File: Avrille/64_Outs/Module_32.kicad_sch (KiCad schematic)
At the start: 9 parts, among them J8 DIN41612_02x32_AC, U6 74HC595, U7 74HC595, U8 74HC595, U9 74HC595

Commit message: reset
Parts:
- added F3: Fuse, Fuse:Fuseholder_Clip-5x20mm_Bel_FC-203-22_Lateral_P17.80x5.00mm_D1.17mm_Horizontal, symbol Device:Fuse
- added RN3, RN5, RN7, RN9: R_Pack08, Package_DIP:DIP-16_W7.62mm, symbol Device:R_Pack08
- C10: renamed from C7; footprint Capacitor_THT:C_Disc_D5.0mm_W2.5mm_P2.50mm -> Capacitor_THT:C_Disc_D4.3mm_W1.9mm_P5.00mm
- C11: renamed from C8; footprint Capacitor_THT:C_Disc_D5.0mm_W2.5mm_P2.50mm -> Capacitor_THT:C_Disc_D4.3mm_W1.9mm_P5.00mm
- C12: renamed from C9; footprint Capacitor_THT:C_Disc_D5.0mm_W2.5mm_P2.50mm -> Capacitor_THT:C_Disc_D4.3mm_W1.9mm_P5.00mm
- C13: renamed from C10; footprint Capacitor_THT:C_Disc_D5.0mm_W2.5mm_P2.50mm -> Capacitor_THT:C_Disc_D4.3mm_W1.9mm_P5.00mm
- U10: renamed from U6; footprint Package_SO:SOIC-16W_7.5x12.8mm_P1.27mm -> Package_DIP:CERDIP-16_W7.62mm_SideBrazed
- U11: renamed from U7; footprint Package_SO:SOIC-16W_7.5x12.8mm_P1.27mm -> Package_DIP:CERDIP-16_W7.62mm_SideBrazed
- U12: renamed from U8; footprint Package_SO:SOIC-16W_7.5x12.8mm_P1.27mm -> Package_DIP:CERDIP-16_W7.62mm_SideBrazed
- U13: renamed from U9; footprint Package_SO:SOIC-16W_7.5x12.8mm_P1.27mm -> Package_DIP:CERDIP-16_W7.62mm_SideBrazed
- renumbered J8 to J9
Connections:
- net GND: no longer J9.a17 (Pin_a17), J9.a18 (Pin_a18), J9.a19 (Pin_a19), J9.a20 (Pin_a20), J9.a21 (Pin_a21), J9.a22 (Pin_a22), J9.a23 (Pin_a23), J9.a24 (Pin_a24), J9.a25 (Pin_a25), J9.a26 (Pin_a26), J9.a27 (Pin_a27), J9.a28 (Pin_a28), J9.a29 (Pin_a29), J9.a30 (Pin_a30), J9.a31 (Pin_a31), J9.a32 (Pin_a32)
- net Sorties_10/IN_1: now also RN9.1 (R1.1); no longer U12.7 (QH)
- net Sorties_10/IN_2: now also RN9.2 (R2.1); no longer U12.6 (QG)
- net Sorties_10/IN_3: now also RN9.3 (R3.1); no longer U12.5 (QF)
- net Sorties_10/IN_4: now also RN9.4 (R4.1); no longer U12.4 (QE)
- net Sorties_10/V_IN: now also F3.1; no longer J9.a1 (Pin_a1), J9.a10 (Pin_a10), J9.a11 (Pin_a11), J9.a12 (Pin_a12), J9.a13 (Pin_a13), J9.a14 (Pin_a14), J9.a15 (Pin_a15), J9.a16 (Pin_a16), J9.a2 (Pin_a2), J9.a3 (Pin_a3), J9.a4 (Pin_a4), J9.a5 (Pin_a5), J9.a6 (Pin_a6), J9.a7 (Pin_a7), J9.a8 (Pin_a8), J9.a9 (Pin_a9)
- net Sorties_11/IN_1: now also RN9.5 (R5.1); no longer U13.7 (QH)
- net Sorties_11/IN_2: now also RN9.6 (R6.1); no longer U13.6 (QG)
- net Sorties_11/IN_3: now also RN9.7 (R7.1); no longer U13.5 (QF)
- net Sorties_11/IN_4: now also RN9.8 (R8.1); no longer U13.4 (QE)
- net Sorties_8/IN_1: now also RN7.1 (R1.1); no longer U10.7 (QH)
- net Sorties_8/IN_2: now also RN7.2 (R2.1); no longer U10.6 (QG)
- net Sorties_8/IN_3: now also RN7.3 (R3.1); no longer U10.5 (QF)
- net Sorties_8/IN_4: now also RN7.4 (R4.1); no longer U10.4 (QE)
- net Sorties_9/IN_1: now also RN7.5 (R5.1); no longer U11.7 (QH)
- net Sorties_9/IN_2: now also RN7.6 (R6.1); no longer U11.6 (QG)
- net Sorties_9/IN_3: now also RN7.7 (R7.1); no longer U11.5 (QF)
- net Sorties_9/IN_4: now also RN7.8 (R8.1); no longer U11.4 (QE)
- net Sorties_10/IN_5: no longer names the net of U12.3 (QD)
- net Sorties_10/IN_5: now also RN7.13 (R4.2)
- net Sorties_10/IN_6: no longer names the net of U12.2 (QC)
- net Sorties_10/IN_6: now also RN7.14 (R3.2)
- net Sorties_10/IN_7: no longer names the net of U12.1 (QB)
- net Sorties_10/IN_7: now also RN7.15 (R2.2)
- net Sorties_10/IN_8: no longer names the net of U12.15 (QA)
- net Sorties_10/IN_8: now also RN7.16 (R1.2)
- net Sorties_11/IN_5: no longer names the net of U13.3 (QD)
- net Sorties_11/IN_5: now also RN9.13 (R4.2)
- net Sorties_11/IN_6: no longer names the net of U13.2 (QC)
- net Sorties_11/IN_6: now also RN9.14 (R3.2)
- net Sorties_11/IN_7: no longer names the net of U13.1 (QB)
- net Sorties_11/IN_7: now also RN9.15 (R2.2)
- net Sorties_11/IN_8: no longer names the net of U13.15 (QA)
- net Sorties_11/IN_8: now also RN9.16 (R1.2)
- net Sorties_8/IN_5: no longer names the net of U10.3 (QD)
- net Sorties_8/IN_5: now also RN3.13 (R4.2)
- net Sorties_8/IN_6: no longer names the net of U10.2 (QC)
- net Sorties_8/IN_6: now also RN3.14 (R3.2)
- net Sorties_8/IN_7: no longer names the net of U10.1 (QB)
- net Sorties_8/IN_7: now also RN3.15 (R2.2)
- net Sorties_8/IN_8: no longer names the net of U10.15 (QA)
- net Sorties_8/IN_8: now also RN3.16 (R1.2)
- net Sorties_9/IN_5: no longer names the net of U11.3 (QD)
- net Sorties_9/IN_5: now also RN5.13 (R4.2)
- net Sorties_9/IN_6: no longer names the net of U11.2 (QC)
- net Sorties_9/IN_6: now also RN5.14 (R3.2)
- net Sorties_9/IN_7: no longer names the net of U11.1 (QB)
- net Sorties_9/IN_7: now also RN5.15 (R2.2)
- net Sorties_9/IN_8: no longer names the net of U11.15 (QA)
- net Sorties_9/IN_8: now also RN5.16 (R1.2)
- new net: RN7.12 (R5.2), U12.4 (QE)
- new net: RN7.11 (R6.2), U12.5 (QF)
- new net: RN7.10 (R7.2), U12.6 (QG)
- new net: RN7.9 (R8.2), U12.7 (QH)
- new net: RN3.12 (R5.2), U10.4 (QE)
- new net: RN3.11 (R6.2), U10.5 (QF)
- new net: RN3.10 (R7.2), U10.6 (QG)
- new net: RN3.9 (R8.2), U10.7 (QH)
- new net: RN9.12 (R5.2), U13.4 (QE)
- new net: RN9.11 (R6.2), U13.5 (QF)
- new net: RN9.10 (R7.2), U13.6 (QG)
- new net: RN9.9 (R8.2), U13.7 (QH)
- new net: RN5.10 (R7.2), U11.6 (QG)
- new net: RN5.11 (R6.2), U11.5 (QF)
- new net: RN5.12 (R5.2), U11.4 (QE)
- new net: RN5.9 (R8.2), U11.7 (QH)
- new net: F3.2, J9.a1 (Pin_a1), J9.a10 (Pin_a10), J9.a11 (Pin_a11), J9.a12 (Pin_a12), J9.a13 (Pin_a13), J9.a14 (Pin_a14), J9.a15 (Pin_a15), J9.a16 (Pin_a16), J9.a17 (Pin_a17), J9.a18 (Pin_a18), J9.a19 (Pin_a19), J9.a2 (Pin_a2), J9.a20 (Pin_a20), J9.a21 (Pin_a21), J9.a22 (Pin_a22), J9.a23 (Pin_a23), J9.a24 (Pin_a24), J9.a25 (Pin_a25), J9.a26 (Pin_a26), J9.a27 (Pin_a27), J9.a28 (Pin_a28), J9.a29 (Pin_a29), J9.a3 (Pin_a3), J9.a30 (Pin_a30), J9.a31 (Pin_a31), J9.a32 (Pin_a32), J9.a4 (Pin_a4), J9.a5 (Pin_a5), J9.a6 (Pin_a6), J9.a7 (Pin_a7), J9.a8 (Pin_a8), J9.a9 (Pin_a9)
- new net Sorties_4/IN_1: RN3.1 (R1.1)
- new net Sorties_4/IN_2: RN3.2 (R2.1)
- new net Sorties_4/IN_3: RN3.3 (R3.1)
- new net Sorties_4/IN_4: RN3.4 (R4.1)
- new net Sorties_5/IN_1: RN3.5 (R5.1)
- new net Sorties_5/IN_2: RN3.6 (R6.1)
- new net Sorties_5/IN_3: RN3.7 (R7.1)
- new net Sorties_5/IN_4: RN3.8 (R8.1)
- new net Sorties_6/IN_1: RN5.1 (R1.1)
- new net Sorties_6/IN_2: RN5.2 (R2.1)
- new net Sorties_6/IN_3: RN5.3 (R3.1)
- new net Sorties_6/IN_4: RN5.4 (R4.1)
- new net Sorties_7/IN_1: RN5.5 (R5.1)
- new net Sorties_7/IN_2: RN5.6 (R6.1)
- new net Sorties_7/IN_3: RN5.7 (R7.1)
- new net Sorties_7/IN_4: RN5.8 (R8.1)
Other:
- added sheet Sorties_4 (Sorties_4.kicad_sch)
- added sheet Sorties_5 (Sorties_4.kicad_sch)
- added sheet Sorties_6 (Sorties_4.kicad_sch)
- added sheet Sorties_7 (Sorties_4.kicad_sch)
- sheet Sorties_10: file Sorties_8.kicad_sch -> Sorties_4.kicad_sch
- sheet Sorties_10 ports: added none; removed IN_5, IN_6, IN_7, IN_8, OUT_5, OUT_6, OUT_7, OUT_8
- sheet Sorties_11: file Sorties_8.kicad_sch -> Sorties_4.kicad_sch
- sheet Sorties_11 ports: added none; removed IN_5, IN_6, IN_7, IN_8, OUT_5, OUT_6, OUT_7, OUT_8
- sheet Sorties_8: file Sorties_8.kicad_sch -> Sorties_4.kicad_sch
- sheet Sorties_8 ports: added none; removed IN_5, IN_6, IN_7, IN_8, OUT_5, OUT_6, OUT_7, OUT_8
- sheet Sorties_9: file Sorties_8.kicad_sch -> Sorties_4.kicad_sch
- sheet Sorties_9 ports: added none; removed IN_5, IN_6, IN_7, IN_8, OUT_5, OUT_6, OUT_7, OUT_8
- title: Carte Midi - 64 Sorties -> Module SPI - 32 Sorties

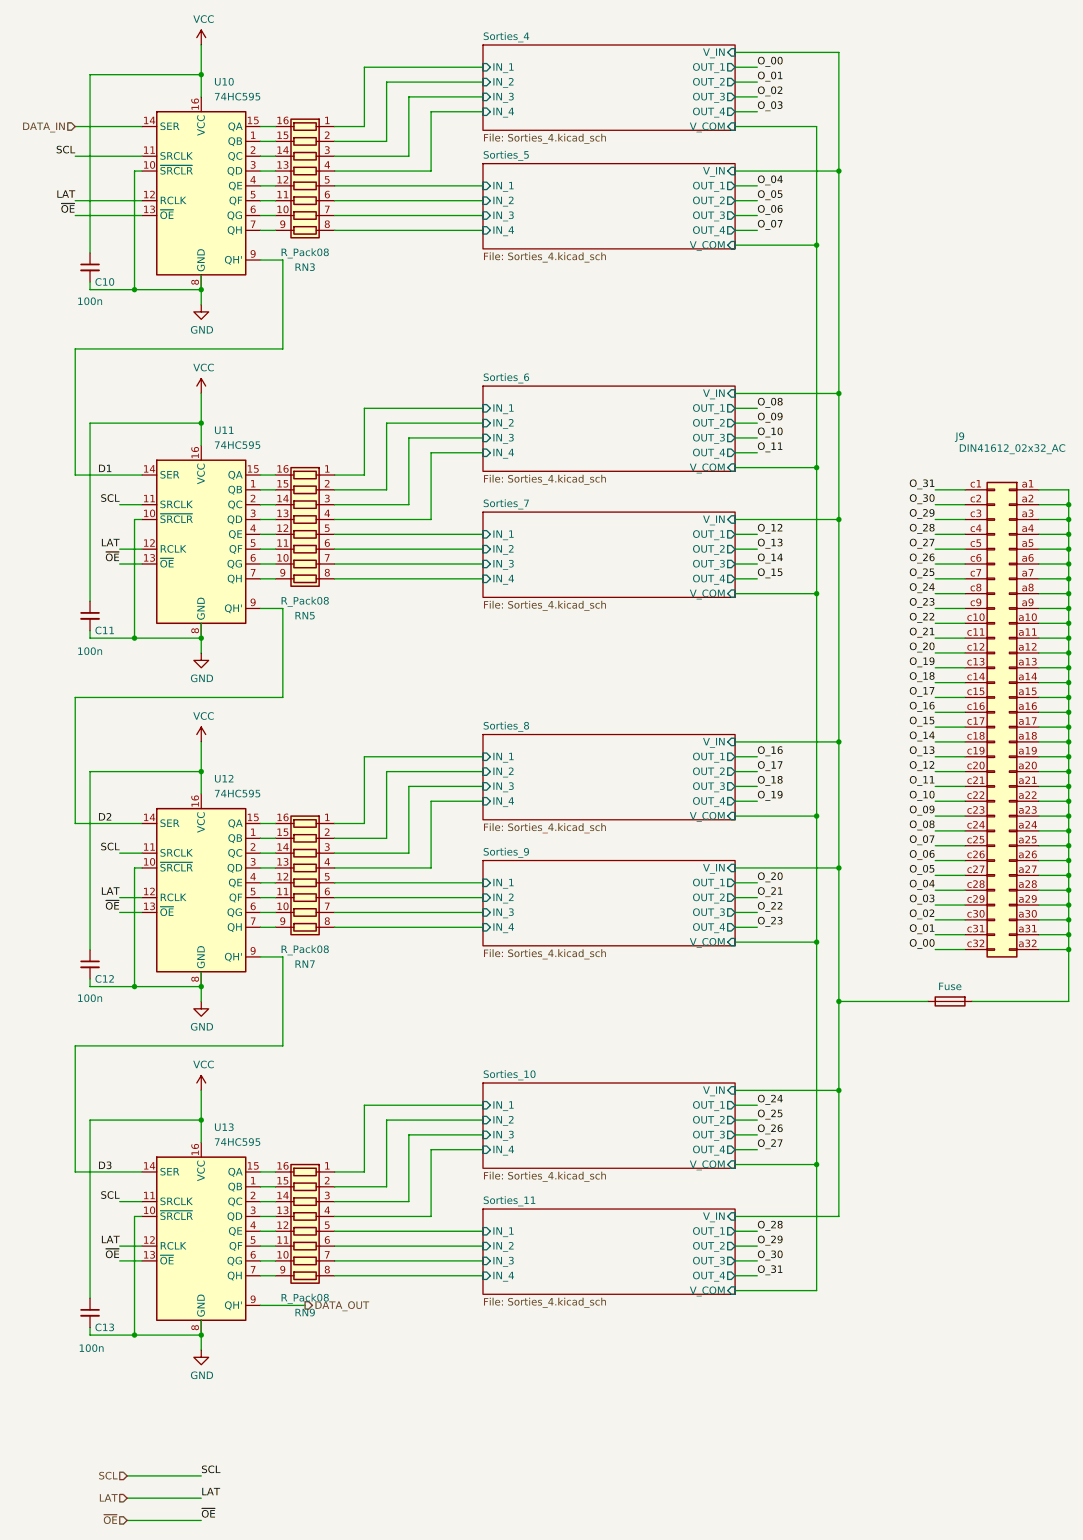
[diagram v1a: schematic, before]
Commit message: Update to SMD Version
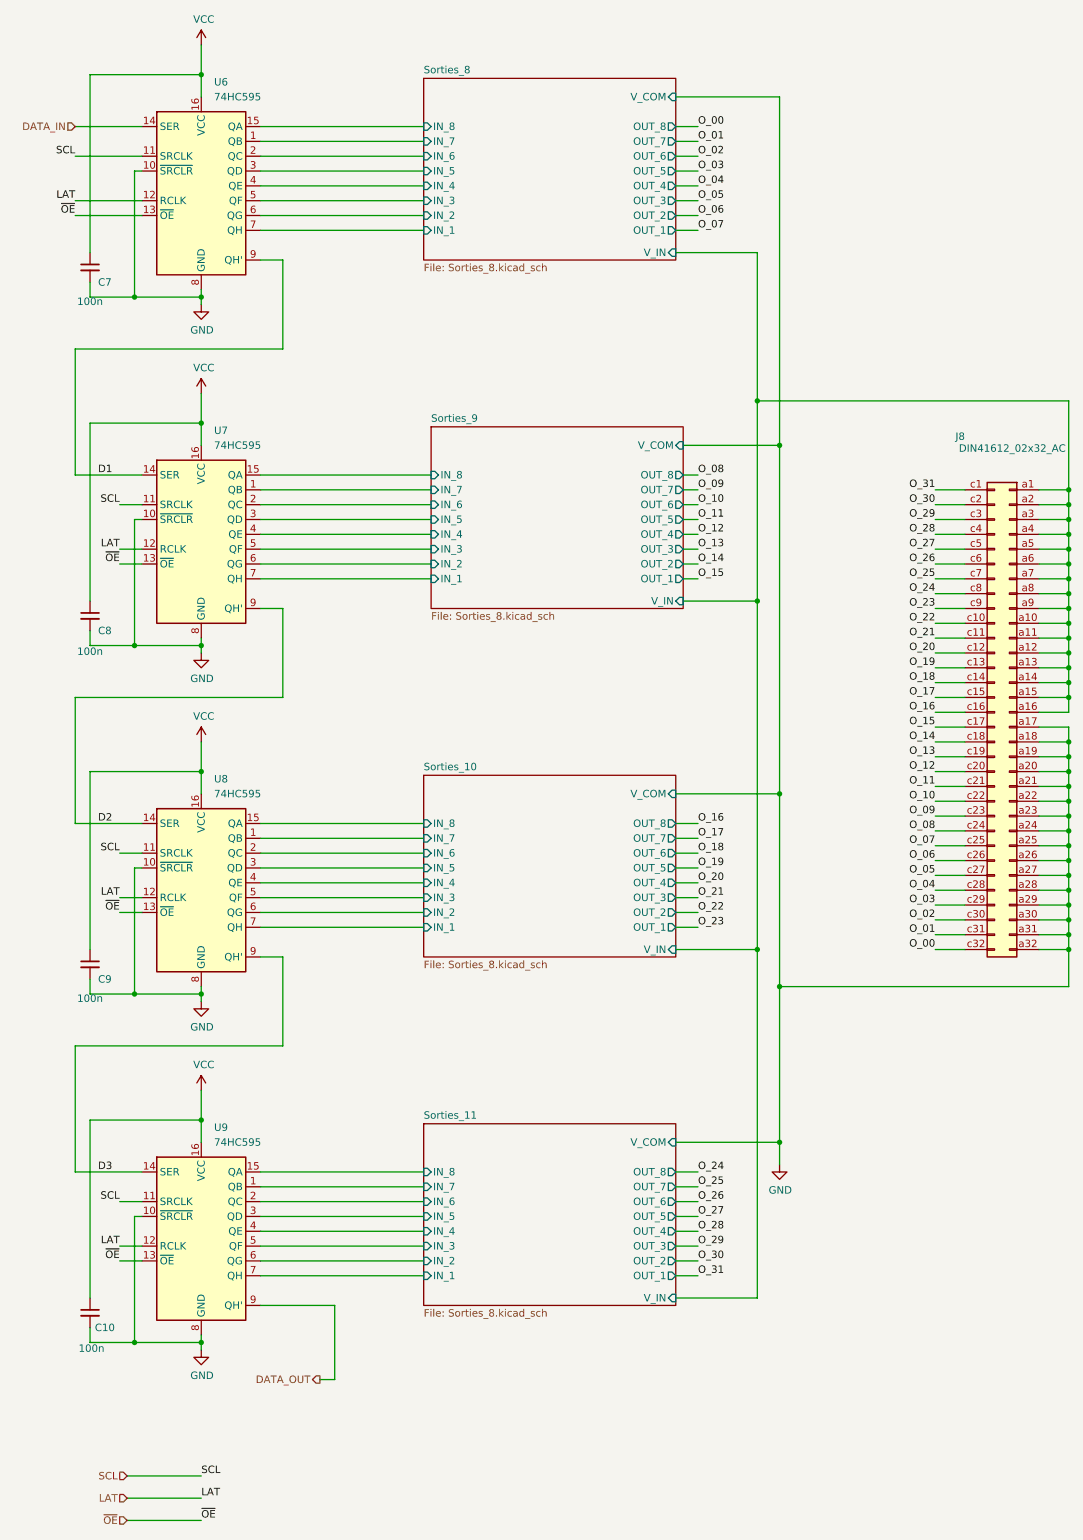
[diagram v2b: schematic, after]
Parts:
- removed F3: Fuse, Fuse:Fuseholder_Clip-5x20mm_Bel_FC-203-22_Lateral_P17.80x5.00mm_D1.17mm_Horizontal, symbol Device:Fuse
- removed RN3, RN5, RN7, RN9: R_Pack08, Package_DIP:DIP-16_W7.62mm, symbol Device:R_Pack08
- C10: renamed from C13; footprint Capacitor_THT:C_Disc_D4.3mm_W1.9mm_P5.00mm -> Capacitor_THT:C_Disc_D5.0mm_W2.5mm_P2.50mm
- C7: renamed from C10; footprint Capacitor_THT:C_Disc_D4.3mm_W1.9mm_P5.00mm -> Capacitor_THT:C_Disc_D5.0mm_W2.5mm_P2.50mm
- C8: renamed from C11; footprint Capacitor_THT:C_Disc_D4.3mm_W1.9mm_P5.00mm -> Capacitor_THT:C_Disc_D5.0mm_W2.5mm_P2.50mm
- C9: renamed from C12; footprint Capacitor_THT:C_Disc_D4.3mm_W1.9mm_P5.00mm -> Capacitor_THT:C_Disc_D5.0mm_W2.5mm_P2.50mm
- U6: renamed from U10; footprint Package_DIP:CERDIP-16_W7.62mm_SideBrazed -> Package_SO:SOIC-16W_7.5x12.8mm_P1.27mm
- U7: renamed from U11; footprint Package_DIP:CERDIP-16_W7.62mm_SideBrazed -> Package_SO:SOIC-16W_7.5x12.8mm_P1.27mm
- U8: renamed from U12; footprint Package_DIP:CERDIP-16_W7.62mm_SideBrazed -> Package_SO:SOIC-16W_7.5x12.8mm_P1.27mm
- U9: renamed from U13; footprint Package_DIP:CERDIP-16_W7.62mm_SideBrazed -> Package_SO:SOIC-16W_7.5x12.8mm_P1.27mm
- renumbered J9 to J8
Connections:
- net GND: now also J8.a17 (Pin_a17), J8.a18 (Pin_a18), J8.a19 (Pin_a19), J8.a20 (Pin_a20), J8.a21 (Pin_a21), J8.a22 (Pin_a22), J8.a23 (Pin_a23), J8.a24 (Pin_a24), J8.a25 (Pin_a25), J8.a26 (Pin_a26), J8.a27 (Pin_a27), J8.a28 (Pin_a28), J8.a29 (Pin_a29), J8.a30 (Pin_a30), J8.a31 (Pin_a31), J8.a32 (Pin_a32)
- net Sorties_10/IN_1: now also U8.7 (QH)
- net Sorties_10/IN_2: now also U8.6 (QG)
- net Sorties_10/IN_3: now also U8.5 (QF)
- net Sorties_10/IN_4: now also U8.4 (QE)
- net Sorties_10/V_IN: now also J8.a1 (Pin_a1), J8.a10 (Pin_a10), J8.a11 (Pin_a11), J8.a12 (Pin_a12), J8.a13 (Pin_a13), J8.a14 (Pin_a14), J8.a15 (Pin_a15), J8.a16 (Pin_a16), J8.a2 (Pin_a2), J8.a3 (Pin_a3), J8.a4 (Pin_a4), J8.a5 (Pin_a5), J8.a6 (Pin_a6), J8.a7 (Pin_a7), J8.a8 (Pin_a8), J8.a9 (Pin_a9)
- net Sorties_11/IN_1: now also U9.7 (QH)
- net Sorties_11/IN_2: now also U9.6 (QG)
- net Sorties_11/IN_3: now also U9.5 (QF)
- net Sorties_11/IN_4: now also U9.4 (QE)
- net Sorties_8/IN_1: now also U6.7 (QH)
- net Sorties_8/IN_2: now also U6.6 (QG)
- net Sorties_8/IN_3: now also U6.5 (QF)
- net Sorties_8/IN_4: now also U6.4 (QE)
- net Sorties_9/IN_1: now also U7.7 (QH)
- net Sorties_9/IN_2: now also U7.6 (QG)
- net Sorties_9/IN_3: now also U7.5 (QF)
- net Sorties_9/IN_4: now also U7.4 (QE)
- net Sorties_10/IN_7: now reaches U8.1 (QB)
- net Sorties_10/IN_8: now reaches U8.15 (QA)
- net Sorties_10/IN_6: now reaches U8.2 (QC)
- net Sorties_10/IN_5: now reaches U8.3 (QD)
- net Sorties_8/IN_7: now reaches U6.1 (QB)
- net Sorties_8/IN_8: now reaches U6.15 (QA)
- net Sorties_8/IN_6: now reaches U6.2 (QC)
- net Sorties_8/IN_5: now reaches U6.3 (QD)
- net Sorties_11/IN_7: now reaches U9.1 (QB)
- net Sorties_11/IN_8: now reaches U9.15 (QA)
- net Sorties_11/IN_6: now reaches U9.2 (QC)
- net Sorties_11/IN_5: now reaches U9.3 (QD)
- net Sorties_9/IN_5: now reaches U7.3 (QD)
- net Sorties_9/IN_6: now reaches U7.2 (QC)
- net Sorties_9/IN_7: now reaches U7.1 (QB)
- net Sorties_9/IN_8: now reaches U7.15 (QA)
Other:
- removed sheet Sorties_4
- removed sheet Sorties_5
- removed sheet Sorties_6
- removed sheet Sorties_7
- sheet Sorties_10: file Sorties_4.kicad_sch -> Sorties_8.kicad_sch
- sheet Sorties_10 ports: added IN_5, IN_6, IN_7, IN_8, OUT_5, OUT_6, OUT_7, OUT_8; removed none
- sheet Sorties_11: file Sorties_4.kicad_sch -> Sorties_8.kicad_sch
- sheet Sorties_11 ports: added IN_5, IN_6, IN_7, IN_8, OUT_5, OUT_6, OUT_7, OUT_8; removed none
- sheet Sorties_8: file Sorties_4.kicad_sch -> Sorties_8.kicad_sch
- sheet Sorties_8 ports: added IN_5, IN_6, IN_7, IN_8, OUT_5, OUT_6, OUT_7, OUT_8; removed none
- sheet Sorties_9: file Sorties_4.kicad_sch -> Sorties_8.kicad_sch
- sheet Sorties_9 ports: added IN_5, IN_6, IN_7, IN_8, OUT_5, OUT_6, OUT_7, OUT_8; removed none
- title: Module SPI - 32 Sorties -> Carte Midi - 64 Sorties
